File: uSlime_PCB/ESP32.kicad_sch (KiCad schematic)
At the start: 12 parts, among them U1 ESP32-C6-MINI-1

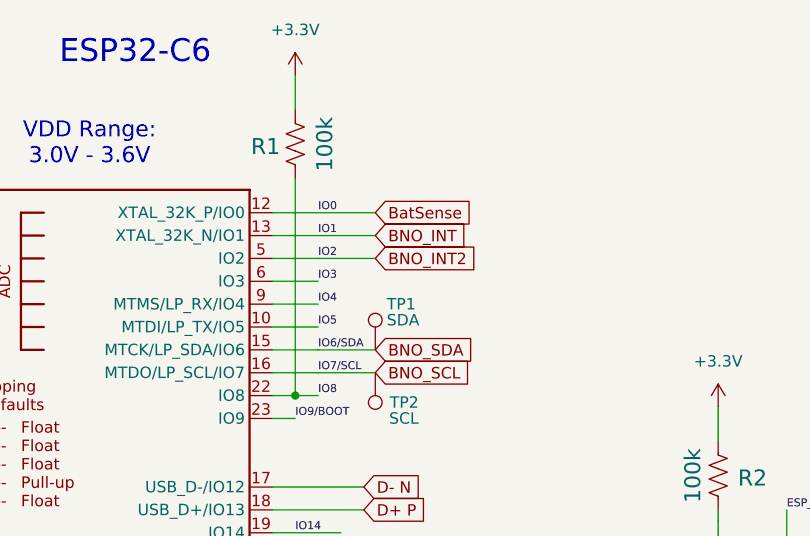
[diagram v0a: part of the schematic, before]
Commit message: Change bat sense pin to not IO0
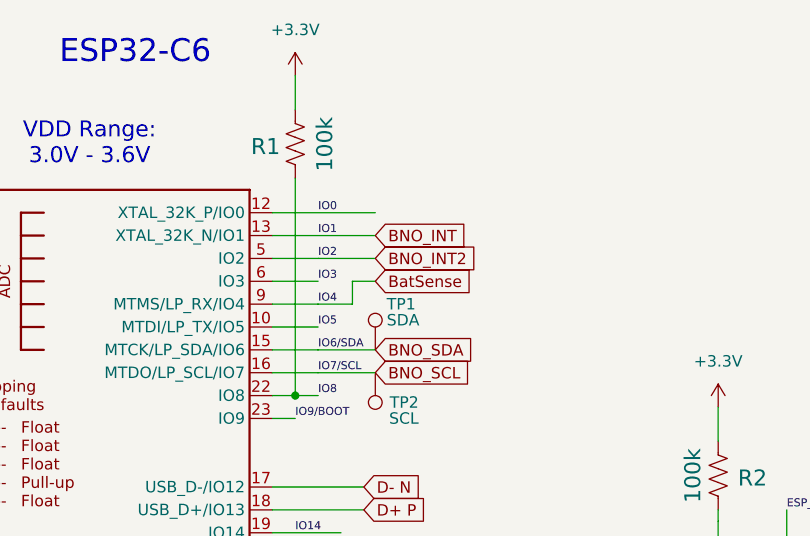
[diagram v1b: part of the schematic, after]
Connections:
- net IO4 is gone; now on net BatSense: U1.9 (MTMS/LP_RX/IO4)
- net BatSense: no longer U1.12 (XTAL_32K_P/IO0)
- new net IO0: U1.12 (XTAL_32K_P/IO0)
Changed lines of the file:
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@@
+	(wire
+		(pts
+			(xy 143.51 82.55) (xy 139.7 82.55)
+		)
+		(stroke
+			(width 0)
+			(type default)
+		)
+	)
 	(wire
 		(pts
@@
 	(wire
 		(pts
+			(xy 146.05 80.01) (xy 143.51 80.01)
+		)
+		(stroke
+			(width 0)
+			(type default)
+		)
+	)
+	(wire
+		(pts
 			(xy 210.82 124.46) (xy 210.82 121.92)
 		)
@@
 		(pts
 			(xy 137.16 125.73) (xy 146.05 125.73)
+		)
+		(stroke
+			(width 0)
+			(type default)
+		)
+	)
+	(wire
+		(pts
+			(xy 143.51 80.01) (xy 143.51 82.55)
 		)
 		(stroke
@@
 	(global_label "BatSense"
 		(shape input)
-		(at 146.05 72.39 0)
+		(at 146.05 80.01 0)
 		(fields_autoplaced yes)
 		(effects
@@
 		)
 		(property "Intersheetrefs" "${INTERSHEET_REFS}"
-			(at 157.7437 72.39 0)
+			(at 157.7437 80.01 0)
 			(effects
 				(font

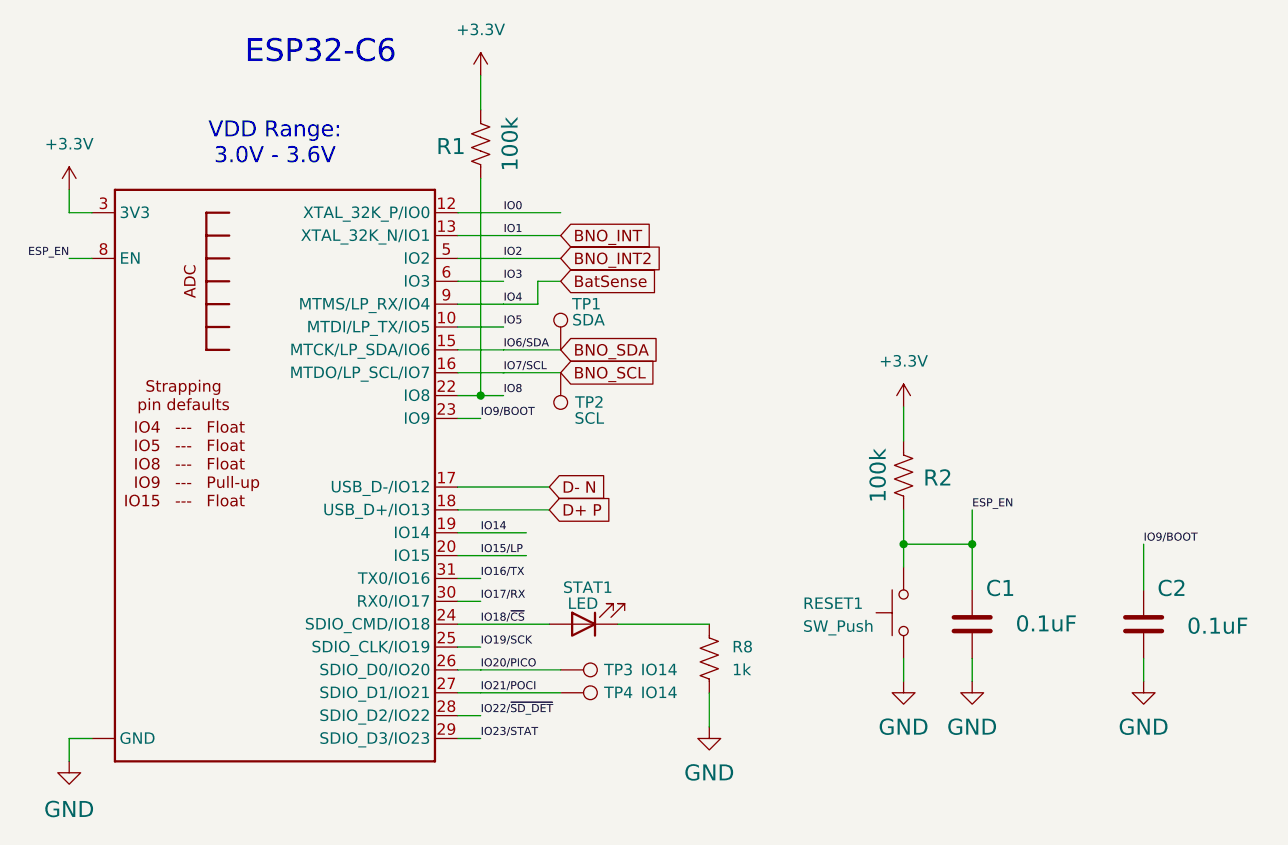
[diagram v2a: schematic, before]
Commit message: v1.0.0 - Use 1206 LED, add resistor pack suggestion
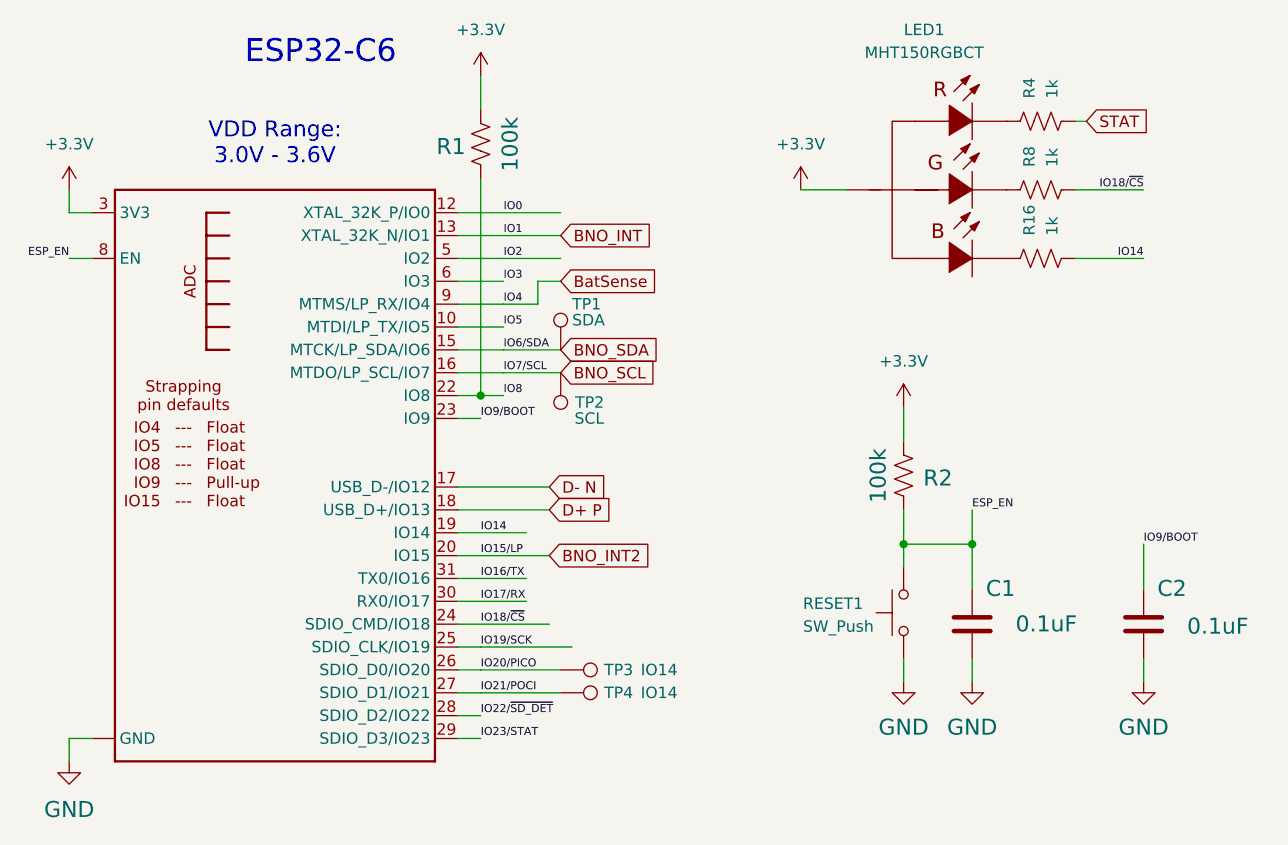
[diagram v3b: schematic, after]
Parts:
- removed STAT1: LED, LED_SMD:LED_0402_1005Metric, symbol uSlime:LED
- added LED1: MHT150RGBCT, uSlime-libs:LED-ARRAY-SMD_1206-4P-L3.2-W1.3-BR-EH, symbol uSlime:MHT150RGBCT
- added R16, R4: 1k, Resistor_SMD:R_0402_1005Metric, symbol uSlime:R_US
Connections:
- net IO15/LP is gone; now on net BNO_INT2: U1.20 (IO15)
- net +3.3V: now also LED1.1 (+)
- net BNO_INT2: no longer U1.5 (IO2)
- net GND: no longer R8.1
- net IO14: now also R16.1
- net IO18/~{CS}: now also R8.1
- net at R8.2: now also LED1.3 (-)
- new net: LED1.2 (-), R16.2
- new net: LED1.4 (-), R4.2
- new net IO2: U1.5 (IO2)
- new net STAT: R4.1

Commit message: Remove GPIO9 capacitor causing boot problems
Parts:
- removed C2: 0.1uF, Capacitor_SMD:C_0402_1005Metric, symbol uSlime:C
- added TP1: BOOT, TestPoint:TestPoint_Pad_D1.0mm, symbol uSlime:TestPoint_Small
- renumbered C1 to C7, R8 to R12, R2 to R6, R4 to R9, TP2 to TP4, TP4 to TP5, TP1 to TP6, U1 to U4
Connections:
- net IO9/BOOT: now also TP1.1
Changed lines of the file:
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@@
-	(wire
-		(pts
-			(xy 210.82 124.46) (xy 210.82 121.92)
-		)
-		(stroke
-			(width 0.1524)
-			(type solid)
-		)
-	)
 	(wire
 		(pts
@@
 	(wire
 		(pts
-			(xy 210.82 109.22) (xy 210.82 114.3)
+			(xy 210.82 109.22) (xy 210.82 123.19)
 		)
 		(stroke
@@
 		(on_board yes)
 		(dnp no)
-		(property "Reference" "U1"
+		(property "Reference" "U4"
 			(at 96.52 67.31 0)
 			(effects
@@
 			(project "uSlime"
 				(path "/f32c1c49-f803-4e7c-a530-6db148a7ba36/27e9da7b-3bfa-4574-a980-93f02fcd8fa2"
-					(reference "U1")
+					(reference "U4")
 					(unit 1)
 				)
@@
 		(on_board yes)
 		(dnp no)
-		(property "Reference" "R4"
+		(property "Reference" "R9"
 			(at 198.1199 59.69 0)
 			(effects
@@
 			(project "uSlime"
 				(path "/f32c1c49-f803-4e7c-a530-6db148a7ba36/27e9da7b-3bfa-4574-a980-93f02fcd8fa2"
-					(reference "R4")
+					(reference "R9")
 					(unit 1)
 				)
@@
 		(on_board yes)
 		(dnp no)
-		(property "Reference" "TP2"
+		(property "Reference" "TP4"
 			(at 150.876 93.472 0)
 			(effects
@@
 			(project "uSlime"
 				(path "/f32c1c49-f803-4e7c-a530-6db148a7ba36/27e9da7b-3bfa-4574-a980-93f02fcd8fa2"
-					(reference "TP2")
+					(reference "TP4")
 					(unit 1)
 				)
@@
 		(on_board yes)
 		(dnp no)
-		(property "Reference" "R8"
+		(property "Reference" "R12"
 			(at 198.1199 67.31 0)
 			(effects
@@
 			(project "uSlime"
 				(path "/f32c1c49-f803-4e7c-a530-6db148a7ba36/27e9da7b-3bfa-4574-a980-93f02fcd8fa2"
-					(reference "R8")
+					(reference "R12")
 					(unit 1)
 				)
@@
 		(on_board yes)
 		(dnp no)
-		(property "Reference" "R2"
+		(property "Reference" "R6"
 			(at 187.96 100.838 0)
 			(effects
@@
 			(project "uSlime"
 				(path "/f32c1c49-f803-4e7c-a530-6db148a7ba36/27e9da7b-3bfa-4574-a980-93f02fcd8fa2"
-					(reference "R2")
+					(reference "R6")
 					(unit 1)
 				)
@@
 	)
 	(symbol
+		(lib_id "uSlime:TestPoint_Small")
+		(at 210.82 123.19 180)
+		(unit 1)
+		(exclude_from_sim no)
+		(in_bom yes)
+		(on_board yes)
+		(dnp no)
+		(property "Reference" "TP1"
+			(at 209.55 128.27 0)
+			(effects
+				(font
+					(size 1.27 1.27)
+				)
+				(justify left)
+			)
+		)
+		(property "Value" "BOOT"
+			(at 209.55 126.492 0)
+			(effects
+				(font
+					(size 1.27 1.27)
+				)
+				(justify left)
+			)
+		)
+		(property "Footprint" "TestPoint:TestPoint_Pad_D1.0mm"
+			(at 205.74 123.19 0)
+			(effects
+				(font
+					(size 1.27 1.27)
+				)
+				(hide yes)
+			)
+		)
+		(property "Datasheet" "~"
+			(at 205.74 123.19 0)
+			(effects
+				(font
+					(size 1.27 1.27)
+				)
+				(hide yes)
+			)
+		)
+		(property "Description" "test point"
+			(at 210.82 123.19 0)
+			(effects
+				(font
+					(size 1.27 1.27)
+				)
+				(hide yes)
+			)
+		)
+		(pin "1"
+		)
+		(instances
+			(project "uSlime"
+				(path "/f32c1c49-f803-4e7c-a530-6db148a7ba36/27e9da7b-3bfa-4574-a980-93f02fcd8fa2"
+					(reference "TP1")
+					(unit 1)
+				)
+			)
+		)
+	)
+	(symbol
 		(lib_id "uSlime:C")
 		(at 191.77 118.11 0)
@@
 		(on_board yes)
 		(dnp no)
-		(property "Reference" "C1"
+		(property "Reference" "C7"
 			(at 193.294 115.189 0)
 			(effects
@@
 			(project "uSlime"
 				(path "/f32c1c49-f803-4e7c-a530-6db148a7ba36/27e9da7b-3bfa-4574-a980-93f02fcd8fa2"
-					(reference "C1")
+					(reference "C7")
 					(unit 1)
 				)
@@
 		(on_board yes)
 		(dnp no)
-		(property "Reference" "TP4"
+		(property "Reference" "TP5"
 			(at 150.876 125.73 90)
 			(effects
@@
 			(project "uSlime"
 				(path "/f32c1c49-f803-4e7c-a530-6db148a7ba36/27e9da7b-3bfa-4574-a980-93f02fcd8fa2"
-					(reference "TP4")
+					(reference "TP5")
 					(unit 1)
 				)
@@
 	)
 	(symbol
-		(lib_id "uSlime:C")
-		(at 210.82 118.11 0)
-		(unit 1)
-		(exclude_from_sim no)
-		(in_bom yes)
-		(on_board yes)
-		(dnp no)
-		(property "Reference" "C2"
-			(at 212.344 115.189 0)
-			(effects
-				(font
-					(size 1.778 1.778)
-				)
-				(justify left bottom)
-			)
-		)
-		(property "Value" "0.1uF"
-			(at 215.646 119.38 0)
-			(effects
-				(font
-					(size 1.778 1.778)
-				)
-				(justify left bottom)
-			)
-		)
-		(property "Footprint" "Capacitor_SMD:C_0402_1005Metric"
-			(at 211.7852 121.92 0)
-			(effects
-				(font
-					(size 1.27 1.27)
-				)
-				(hide yes)
-			)
-		)
-		(property "Datasheet" "~"
-			(at 210.82 118.11 0)
-			(effects
-				(font
-					(size 1.27 1.27)
-				)
-				(hide yes)
-			)
-		)
-		(property "Description" "Unpolarized capacitor"
-			(at 210.82 118.11 0)
-			(effects
-				(font
-					(size 1.27 1.27)
-				)
-				(hide yes)
-			)
-		)
-		(pin "1"
-		)
-		(pin "2"
-		)
-		(instances
-			(project "uSlime"
-				(path "/f32c1c49-f803-4e7c-a530-6db148a7ba36/27e9da7b-3bfa-4574-a980-93f02fcd8fa2"
-					(reference "C2")
-					(unit 1)
-				)
-			)
-		)
-	)
-	(symbol
 		(lib_id "uSlime:TestPoint")
 		(at 146.05 123.19 270)
@@
 		(on_board yes)
 		(dnp no)
-		(property "Reference" "TP1"
+		(property "Reference" "TP6"
 			(at 147.32 82.55 0)
 			(effects
@@
 			(project "uSlime"
 				(path "/f32c1c49-f803-4e7c-a530-6db148a7ba36/27e9da7b-3bfa-4574-a980-93f02fcd8fa2"
-					(reference "TP1")
+					(reference "TP6")
 					(unit 1)
 				)
@@
 					(unit 1)
 				)
-			)
-		)
-	)
-	(symbol
-		(lib_id "power:GND")
-		(at 210.82 124.46 0)
-		(unit 1)
-		(exclude_from_sim no)
-		(in_bom yes)
-		(on_board yes)
-		(dnp no)
-		(property "Reference" "#GND05"
-			(at 210.82 124.46 0)
-			(effects
-				(font
-					(size 1.27 1.27)
-				)
-				(hide yes)
-			)
-		)
-		(property "Value" "GND"
-			(at 210.82 128.524 0)
-			(effects
-				(font
-					(size 1.778 1.778)
-				)
-				(justify top)
-			)
-		)
-		(property "Footprint" ""
-			(at 210.82 124.46 0)
-			(effects
-				(font
-					(size 1.27 1.27)
-				)
-				(hide yes)
-			)
-		)
-		(property "Datasheet" ""
-			(at 210.82 124.46 0)
-			(effects
-				(font
-					(size 1.27 1.27)
-				)
-				(hide yes)
-			)
-		)
-		(property "Description" "Power symbol creates a global label with name \"GND\" , ground"
-			(at 210.82 124.46 0)
-			(effects
-				(font
-					(size 1.27 1.27)
-				)
-				(hide yes)
-			)
-		)
-		(pin "1"
-		)
-		(instances
-			(project "uSlime"
-				(path "/f32c1c49-f803-4e7c-a530-6db148a7ba36/27e9da7b-3bfa-4574-a980-93f02fcd8fa2"
-					(reference "#GND05")
-					(unit 1)
-				)
